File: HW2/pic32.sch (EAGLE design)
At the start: 11 parts, among them J1 USB-MB-H

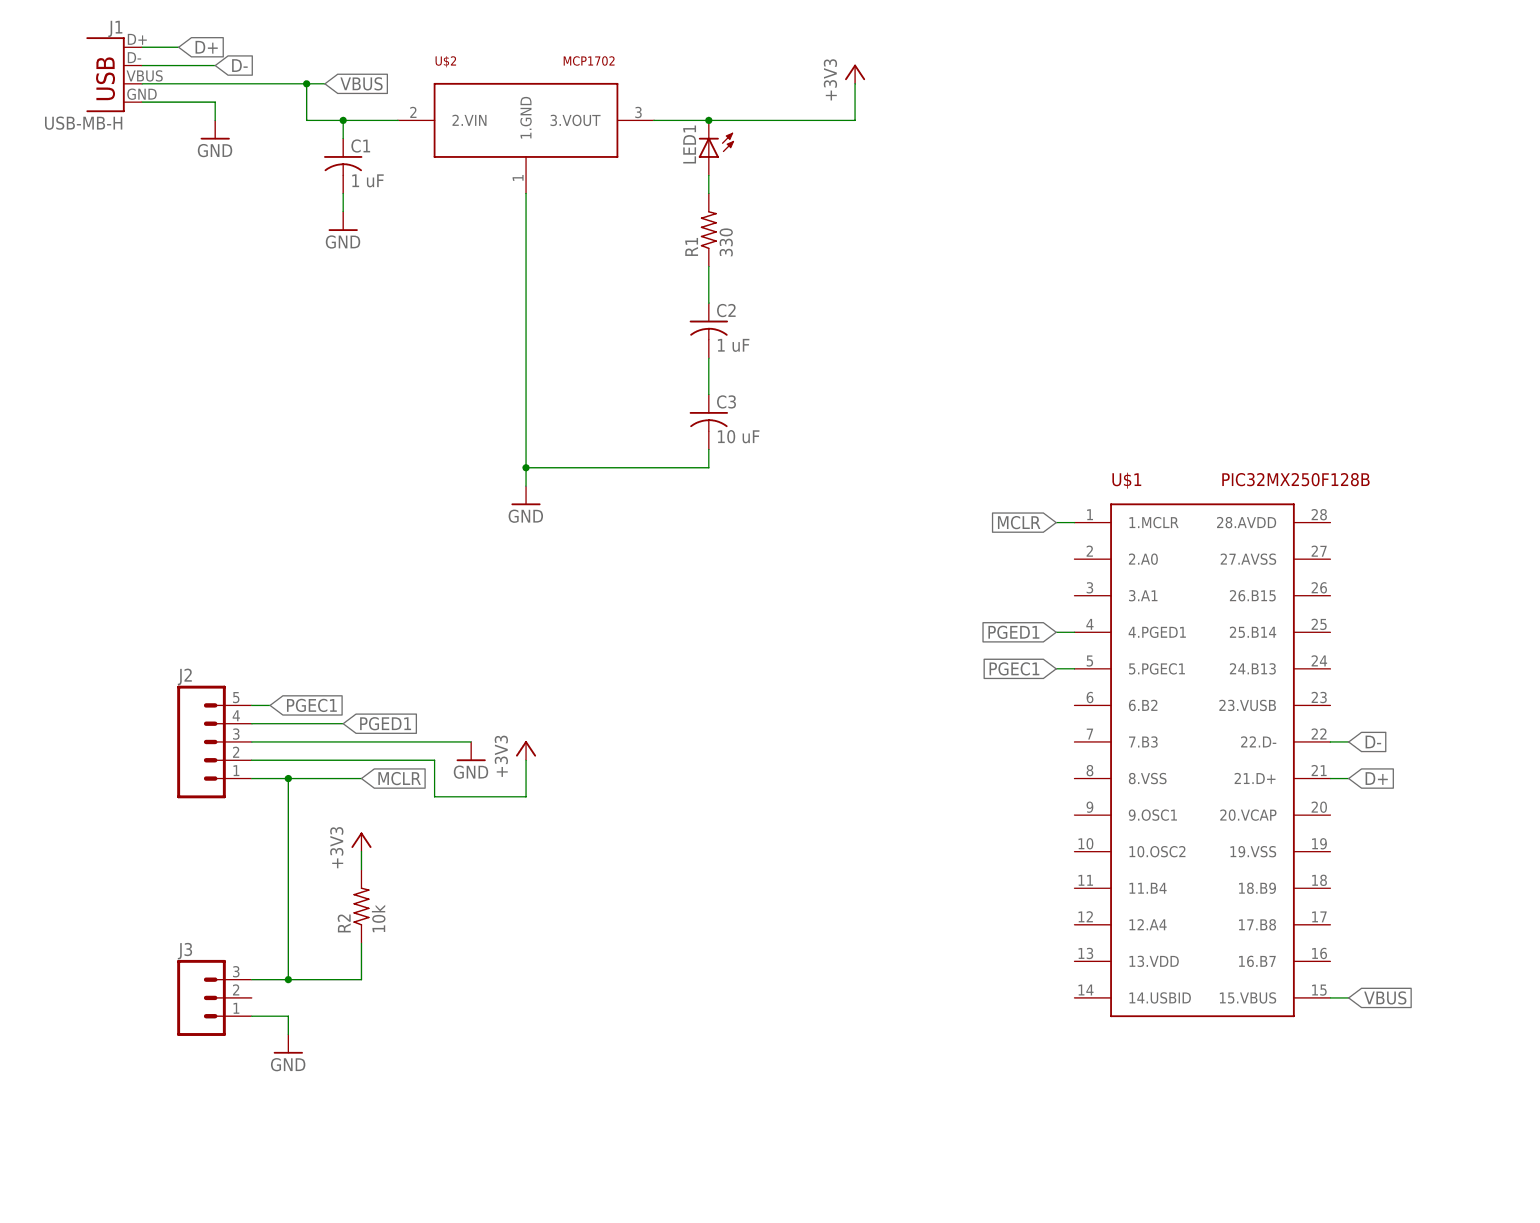
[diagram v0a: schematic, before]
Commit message: Added buttons, LED, oscillator, etc
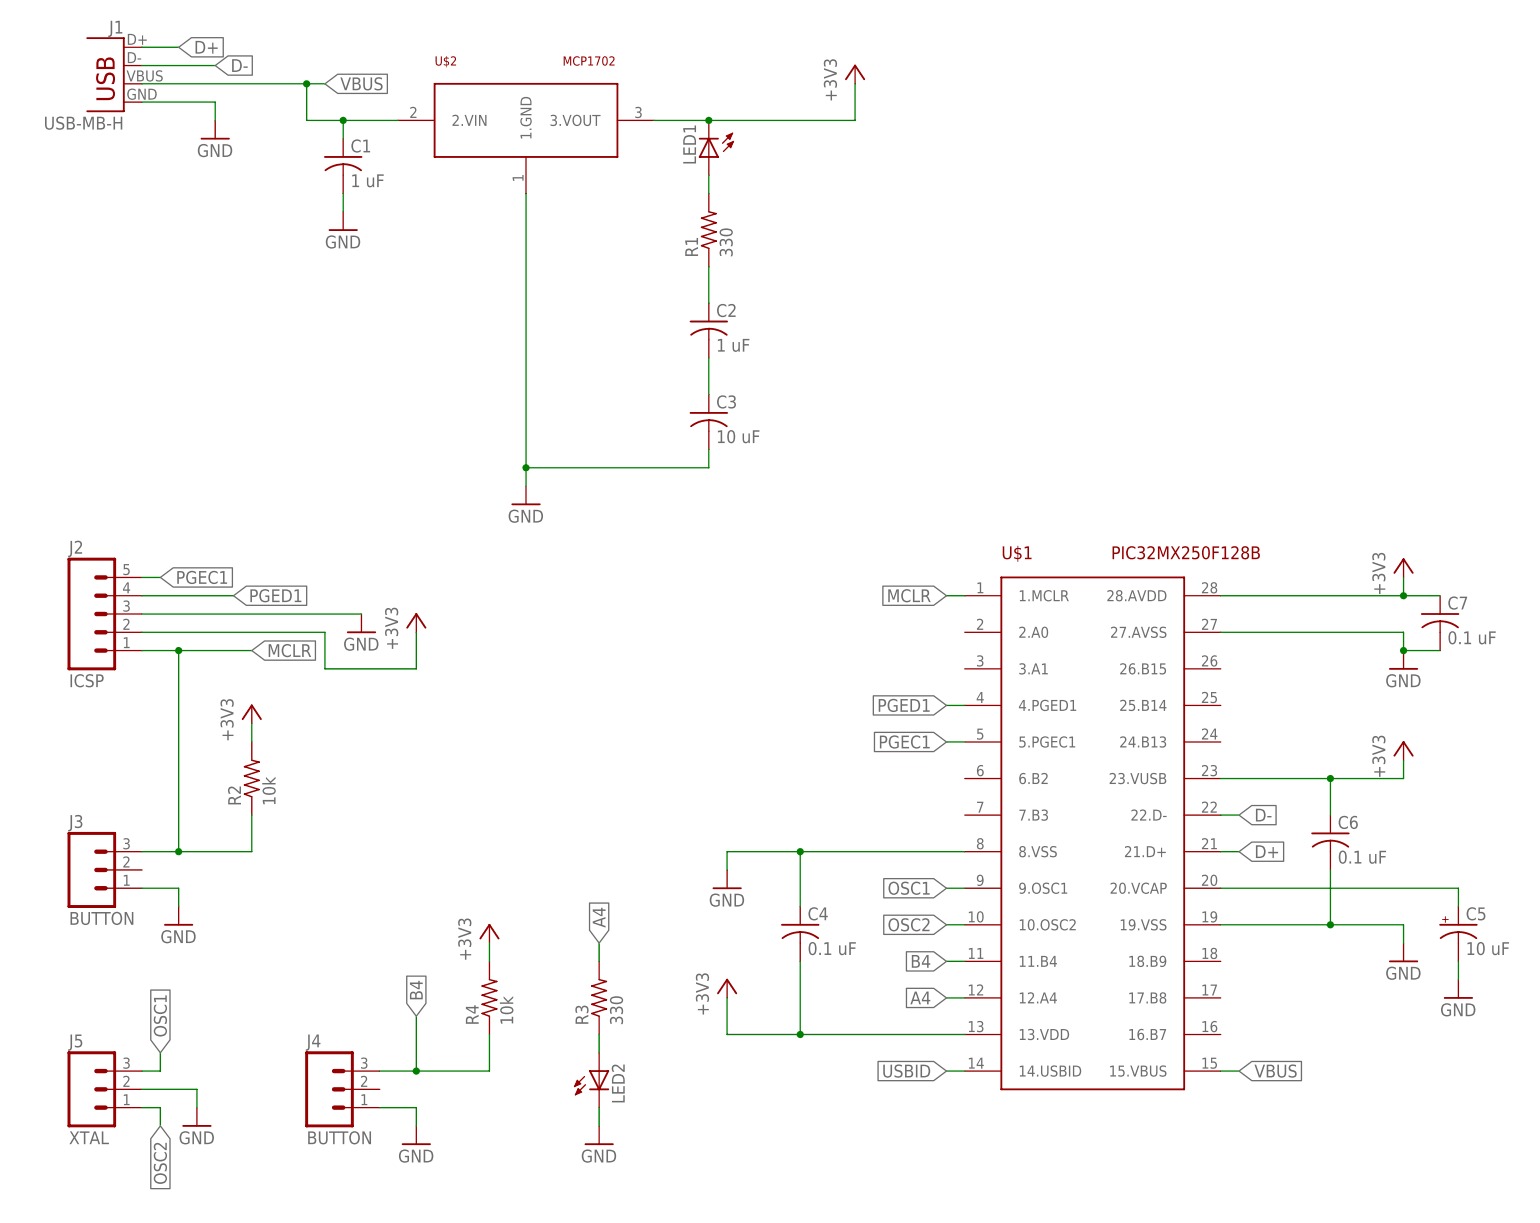
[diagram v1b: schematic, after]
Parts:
- added C4, C6, C7: 0.1 uF, me433:C-US025-024X044
- added C5: 10 uF, me433:CPOL-USE1.8-4
- added J4: BUTTON, me433:M03PTH
- added J5: XTAL, me433:M03PTH
- added LED2: (no value), me433:LED3MM
- added R3: 330, me433:R-US_0207/10
- added R4: 10k, me433:R-US_0207/10
- J2: value (none) -> ICSP
- J3: value (none) -> BUTTON
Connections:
- new net A4: R3.2, U$1.12.A4
- new net B4: J4.3, R4.1, U$1.11.B4
- new net N$4: C5.+, U$1.20.VCAP
- new net N$5: LED2.A, R3.1
- new net OSC1: J5.3, U$1.9.OSC1
- new net OSC2: J5.1, U$1.10.OSC2
- new net USBID: U$1.14.USBID
- net +3V3: now also C4.2, C6.1, C7.1, R4.2, U$1.13.VDD, U$1.23.VUSB, U$1.28.AVDD
- net GND: now also C4.1, C5.-, C6.2, C7.2, J4.1, J5.2, LED2.C, U$1.19.VSS, U$1.27.AVSS, U$1.8.VSS
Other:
- moved on the sheet: J2, J3, R2, U$1
